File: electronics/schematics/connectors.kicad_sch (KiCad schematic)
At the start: 2 parts, among them J1 Audio Jack TRS, 6pin (with sw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, J2 Audio Jack TRS, 6pin (with sw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

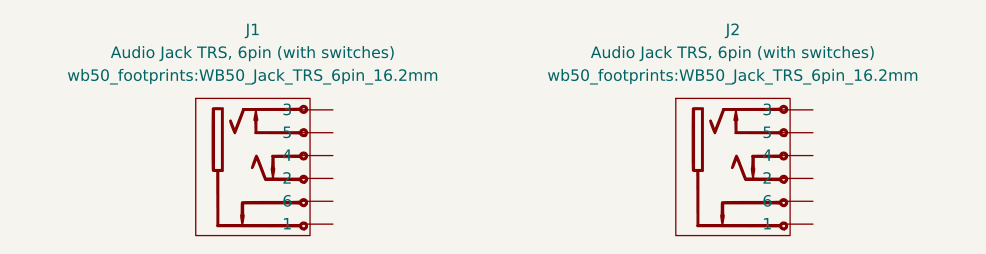
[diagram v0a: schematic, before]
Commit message: frontpanel parts placed and locked
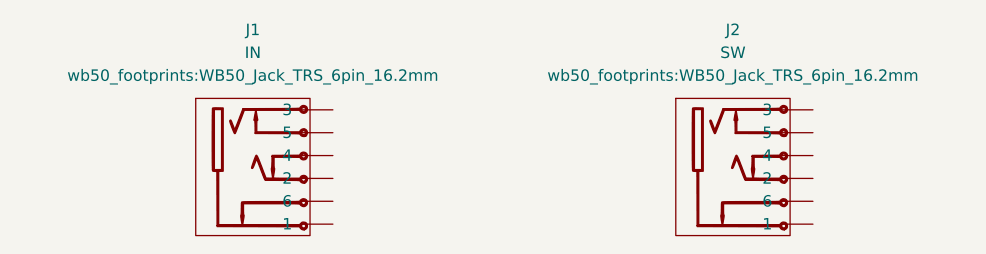
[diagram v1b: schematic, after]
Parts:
- J1: value Audio Jack TRS, 6pin (with switches) -> IN
- J2: value Audio Jack TRS, 6pin (with switches) -> SW
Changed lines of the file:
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@@
 			)
 		)
-		(property "Value" "Audio Jack TRS, 6pin (with switches)"
+		(property "Value" "IN"
 			(at 96.52 64.77 0)
 			(effects
@@
 			)
 		)
-		(property "Value" "Audio Jack TRS, 6pin (with switches)"
+		(property "Value" "SW"
 			(at 149.86 64.77 0)
 			(effects
